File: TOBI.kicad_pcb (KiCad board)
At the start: 4 copper layers, 23 parts, among them J1 Battery Connector, J2 Top Screw Terminal, J3 Bottom Screw Terminal, Q1 Q_NMOS_GDS, Q2 Q_NMOS_GDS, Q3 Q_NMOS_GDS, U1 XIAO-ESP32-S3-SMD, U2 LSM6DSO32, U4 MS5611-01BA

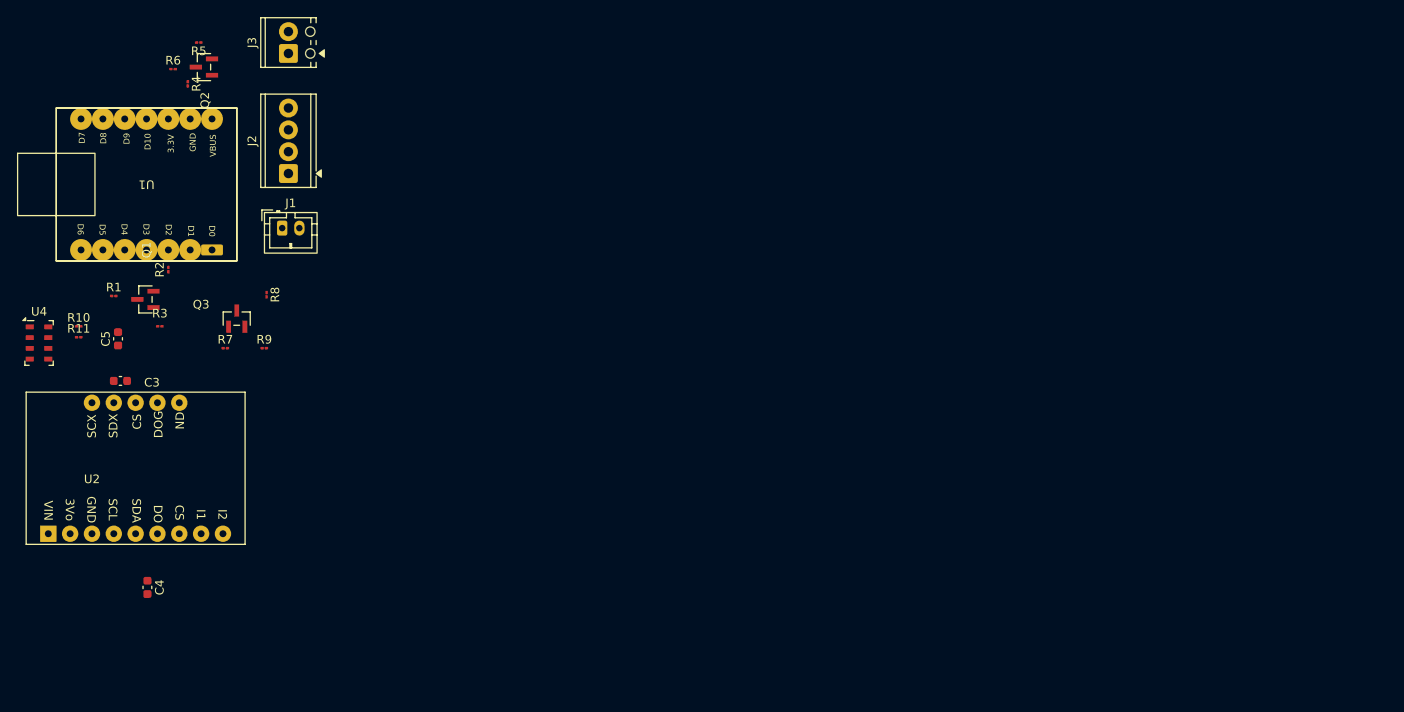
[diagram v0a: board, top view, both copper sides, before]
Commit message: PCB Design Fixes from Andrew
Meeting notes: PCB design considerations:
Can go a hair bigger on track width with the smaller pads; 0.5/0.6

Front:
Make the trace around the threaded rod more of a 45º than 90º
Middle
Go through the middle rather than around the bend
Possibly fix the bottom battery terminal

Back:
Top - also make those 45º (right)
Trace pad 1 & 3 up and 2 on the bottom? Could have tracing
Same with far left clean up a little bit
Clear out kinks with pad1 on dso? Could be fixed regardless when fixing other traces around there

Get stencil with PCB when ordering
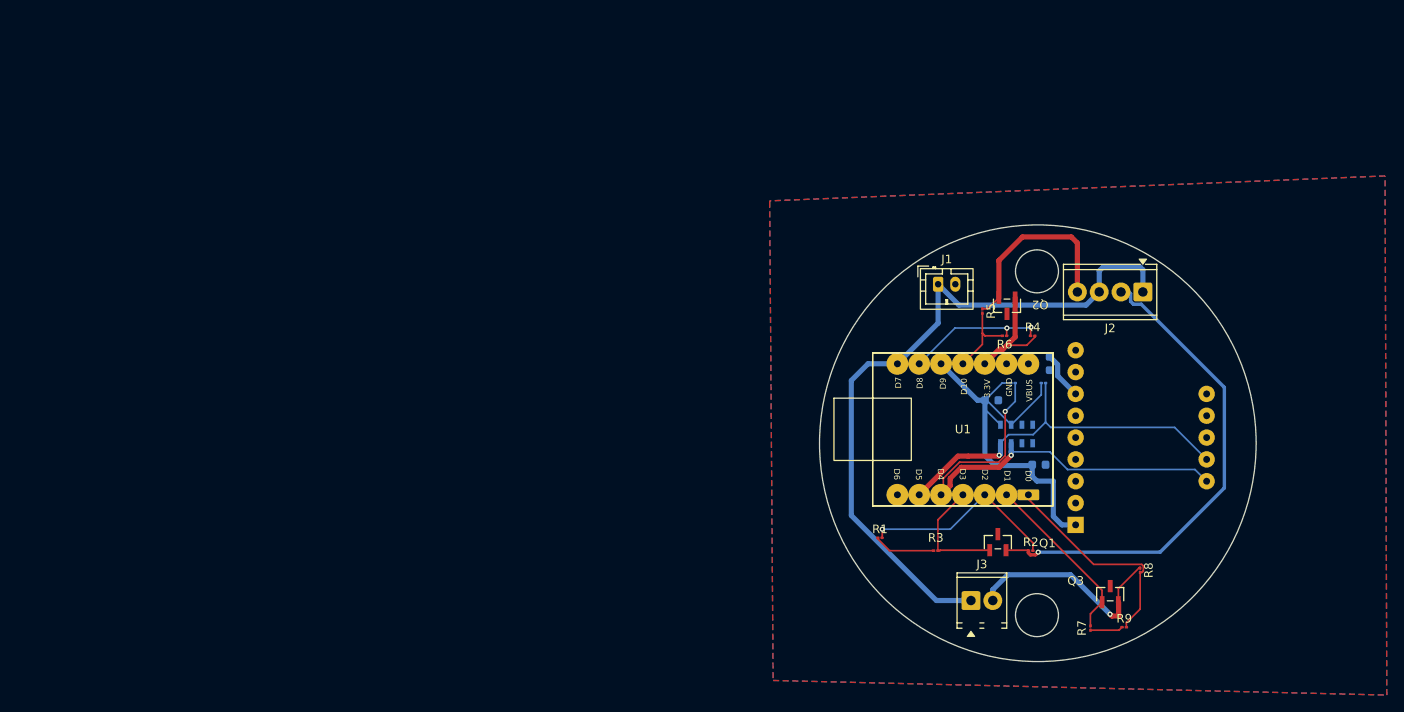
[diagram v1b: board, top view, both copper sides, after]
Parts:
- C3, C4, C5, R10, R11, U2, U4: moved to B.Cu
- moved U2 117.0 mm to (204.6, 101.8), turned to 90 degrees
- moved U4 114.2 mm to (190.1, 101.4), turned to -90 degrees
- moved R10 112.4 mm to (193.2, 95.5)
- moved R11 108.9 mm to (189.7, 95.5)
- moved C4 108.2 mm to (194.0, 93.2), turned to 90 degrees
- moved C5 108.1 mm to (192.7, 105.0), turned to 180 degrees
- moved Q3 106.6 mm to (201.0, 120.1)
- moved R8 106.6 mm to (204.5, 117.3)
- moved R7 105.8 mm to (198.7, 124.0), turned to 90 degrees
- moved R2 105.5 mm to (191.8, 115.0), turned to 0 degrees
- moved R9 105.2 mm to (202.7, 123.9)
- moved Q1 103.1 mm to (188.0, 114.0), turned to 0 degrees
- moved R4 102.6 mm to (192.0, 90.0), turned to 0 degrees
- moved J3 101.8 mm to (184.8, 120.8), turned to 0 degrees
- moved R6 101.6 mm to (188.7, 90.0), turned to 180 degrees
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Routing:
- net +BATT: track 0.00 -> 81.9 mm
- net /APPO: track 0.00 -> 57.9 mm, vias 0 -> 1
- net /SDA: track 0.00 -> 56.4 mm, vias 0 -> 2
- net +3.3V: track 0.00 -> 48.6 mm
- net /SCL: track 0.00 -> 44.0 mm, vias 0 -> 1
- net GND: track 0.00 -> 27.7 mm, vias 0 -> 2
- net /MOTOR: track 0.00 -> 25.3 mm, vias 0 -> 1
- net /CONT 3: track 0.00 -> 25.2 mm
- net /CONT 1: track 0.00 -> 23.4 mm, vias 0 -> 1
- net /MAIN: track 0.00 -> 23.0 mm
- net /IGNIT 3: track 0.00 -> 20.4 mm
- net /IGNIT 1: track 0.00 -> 13.7 mm
- net /IGNIT 2: track 0.00 -> 13.2 mm
- net /CONT 2: track 0.00 -> 9.29 mm
- net Net-(U2-INT1): track 0.00 -> 5.55 mm
- added copper zone on B.Cu, net GND
- added copper zone on F.Cu, net GND
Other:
- board outline added: 50.8 x 50.8 mm

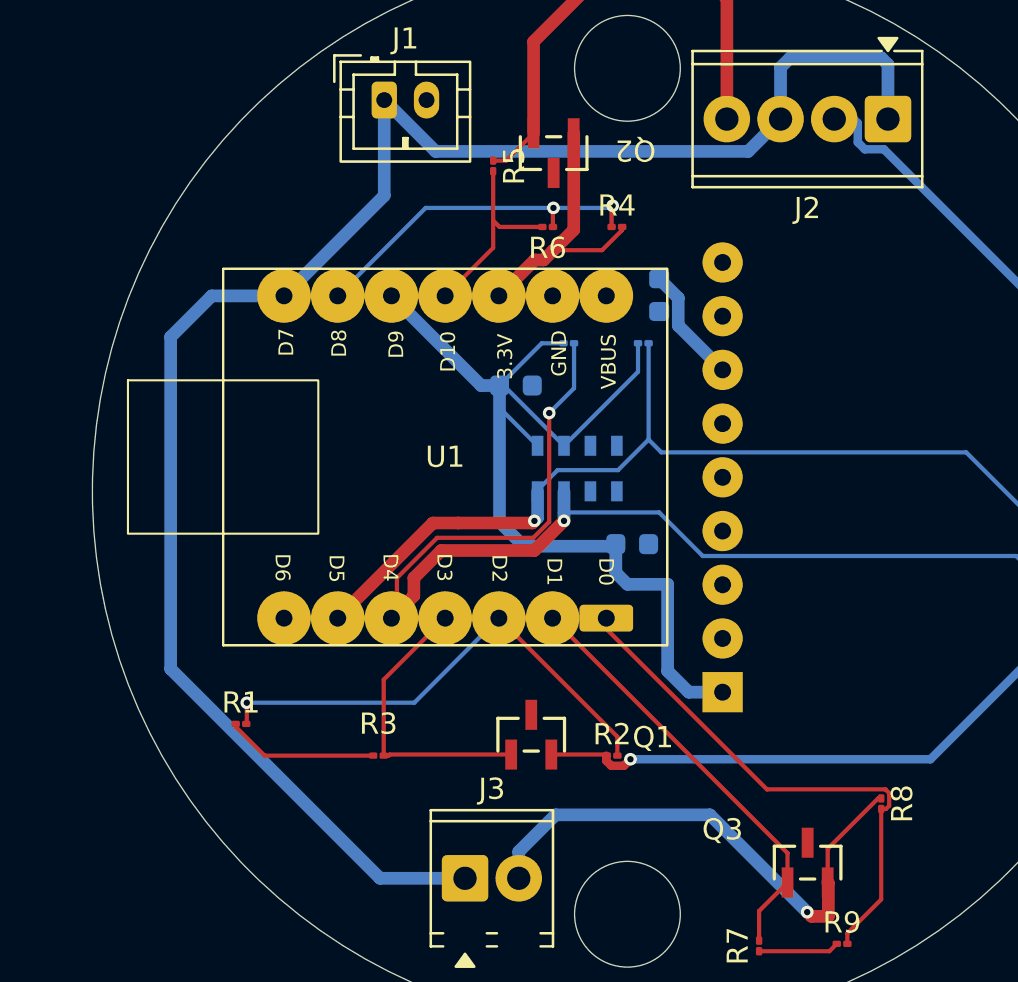
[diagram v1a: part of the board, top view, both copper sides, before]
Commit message: Modified ESP32S3 Footprint
Incorrect footprint for the ESP, updated and modified the PCB for re-wiring.
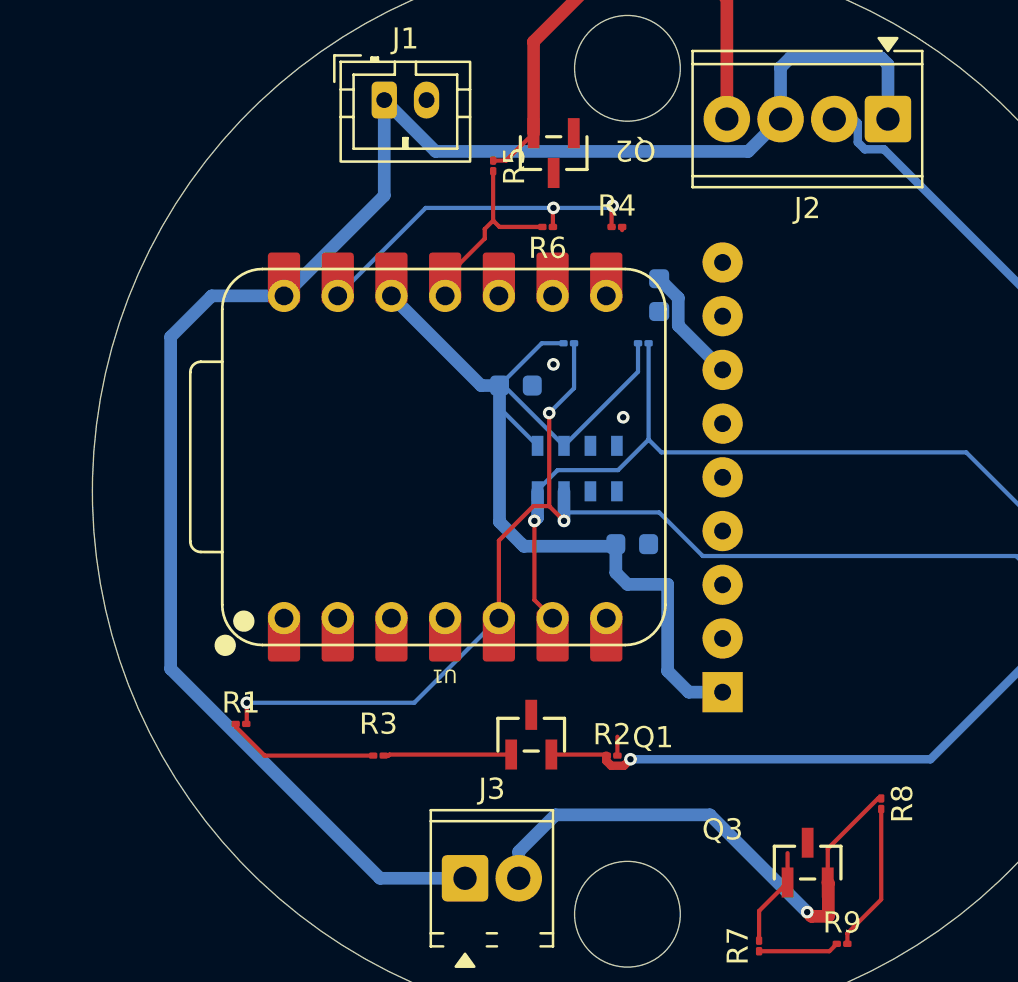
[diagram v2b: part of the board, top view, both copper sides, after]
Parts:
- U1: footprint Library:ESP32S3 -> Seeed_Studio_XIAO_Series:XIAO-ESP32-S3-DIP
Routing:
- net /CONT 3: track 25.2 -> 7.54 mm
- net /IGNIT 3: track 20.4 -> 4.70 mm
- net /SDA: track 56.4 -> 41.1 mm
- net /IGNIT 2: track 13.2 -> 0.15 mm
- net /IGNIT 1: track 13.7 -> 6.05 mm
- net /CONT 1: track 23.4 -> 15.8 mm
- net /SCL: track 44.0 -> 37.5 mm
- net /CONT 2: track 9.29 -> 8.45 mm
- net GND: vias 2 -> 4

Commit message: Updated Wiring
Semi-final wiring for PCB.
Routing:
- net /CONT 3: track 7.54 -> 45.0 mm, vias 0 -> 2
- net /IGNIT 3: track 4.70 -> 31.5 mm
- net /IGNIT 2: track 0.15 -> 12.3 mm
- net /CONT 1: track 15.8 -> 24.7 mm, vias 1 -> 3
- net /IGNIT 1: track 6.05 -> 12.3 mm, vias 0 -> 2
